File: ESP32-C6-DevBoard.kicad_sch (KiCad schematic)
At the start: 49 parts, among them J1 USB_C_Receptacle_USB2.0_16P, J2 Conn_01x02_Pin, J4 USB_C_Receptacle_USB2.0_16P, J5 Conn_01x16_Pin, J6 Conn_01x16_Pin, Q1 BC847, Q2 BC847, U1 ESP32-C6-MINI-1, U2 CP2104, U3 TLV75801PDRV

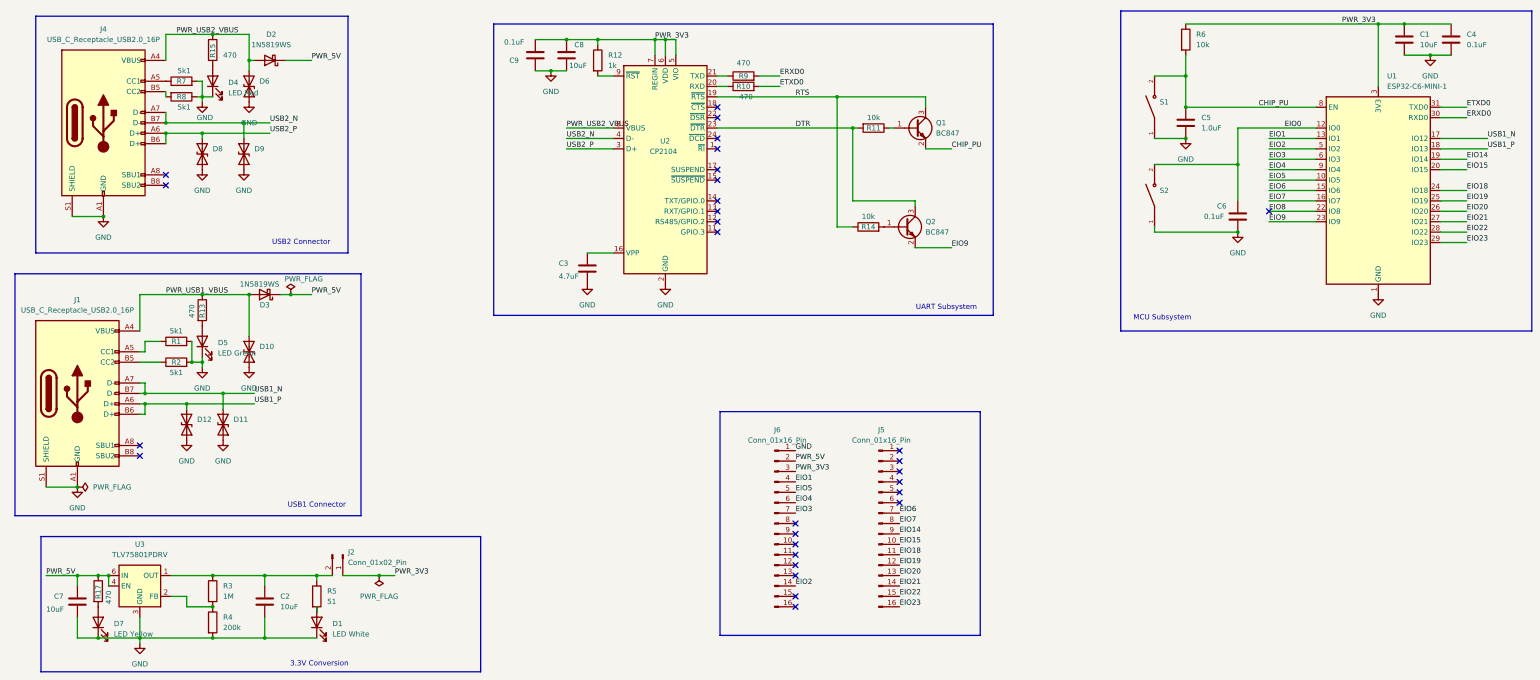
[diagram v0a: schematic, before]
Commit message: Changed to better USB-C connector footprint. Reduced size Changed to 1A 3.3V converter
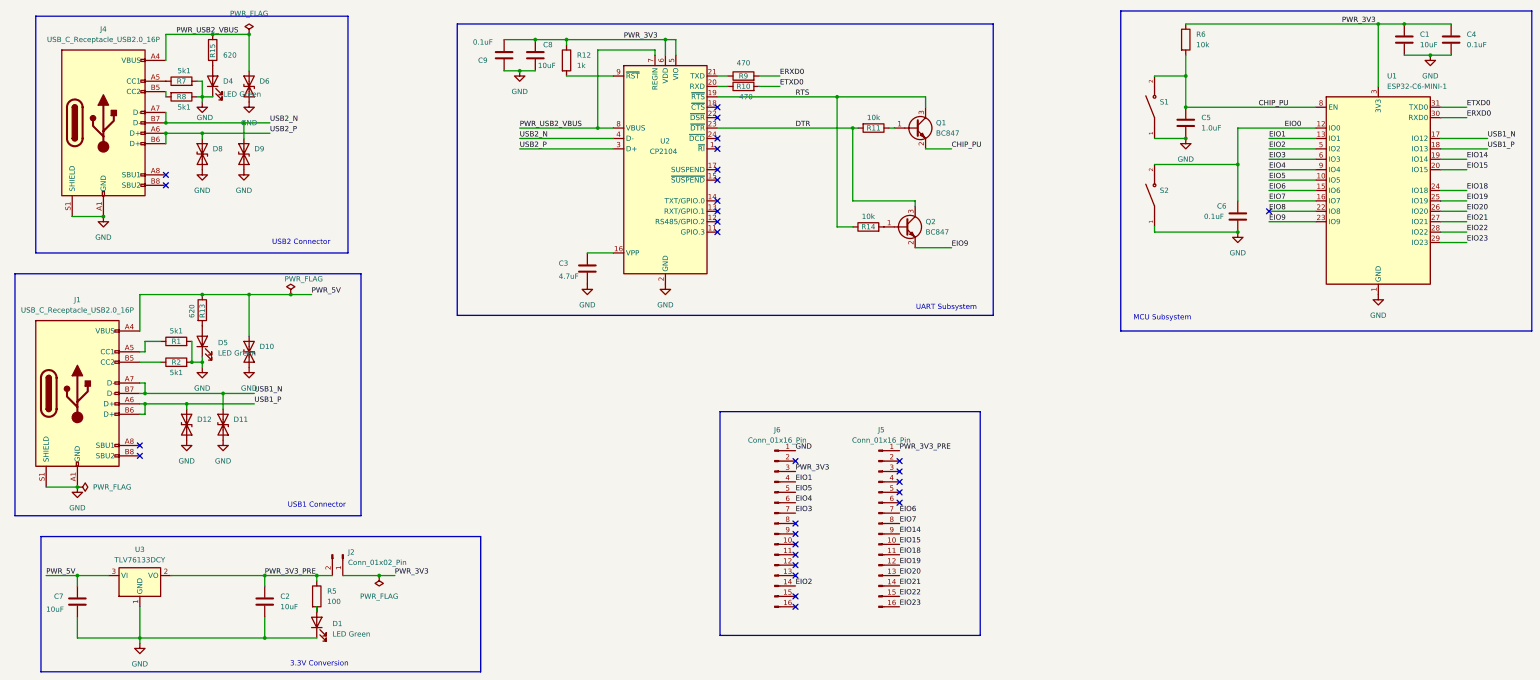
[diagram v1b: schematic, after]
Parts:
- removed D2, D3: 1N5819WS, Diode_SMD:D_SOD-323, symbol Diode:1N5819WS
- removed D7: LED Yellow, LED_SMD:LED_0603_1608Metric, symbol Device:LED
- removed R17: 470, Resistor_SMD:R_0603_1608Metric, symbol Device:R
- removed R3: 1M, Resistor_SMD:R_0603_1608Metric, symbol Device:R
- removed R4: 200k, Resistor_SMD:R_0603_1608Metric, symbol Device:R
- removed U3: TLV75801PDRV, Package_SON:WSON-6-1EP_2x2mm_P0.65mm_EP1x1.6mm, symbol Regulator_Linear:TLV75801PDRV
- added U3: TLV76133DCY, Package_TO_SOT_SMD:SOT-223-3_TabPin2, symbol Regulator_Linear:TLV76133DCY
- D1: value LED White -> LED Green; LCSC C2290 -> C12065; LCSC Part Name C125123 -> C12065
- D4: value LED Red -> LED Green; LCSC C2286 -> C12065; LCSC Part Name C125103 -> C12065
- D5: LCSC C916074 -> C12065
- J1, J4: footprint Connector_USB:USB_C_Receptacle_JAE_DX07S016JA1R1500 -> Connector_USB:USB_C_Receptacle_HRO_TYPE-C-31-M-12
- R13, R15: value 470 -> 620; LCSC C23179 -> C23220; LCSC Part Name C23197 -> C23220
- R5: value 51 -> 100; LCSC C23197 -> C22775; LCSC Part Name C23197 -> C22775
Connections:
- net PWR_USB1_VBUS is gone; now on net PWR_5V: D10.2 (A2), J1.A4 (VBUS), J1.A9 (VBUS), J1.B4 (VBUS), J1.B9 (VBUS), R13.1
- net GND: now also U3.1 (GND)
- net PWR_3V3: no longer U2.7 (REGIN)
- net PWR_5V: now also U3.3 (VI); no longer J6.2 (Pin_2)
- net PWR_USB2_VBUS: now also U2.7 (REGIN)
- net PWR_3V3_PRE: now reaches C2.1, J2.2 (Pin_2), R5.1
- net PWR_3V3_PRE: now also J5.1 (Pin_1), U3.2 (VO)
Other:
- moved on the sheet: C8, C9, R12

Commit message: Further improvements
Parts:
- C1, C2, C7, C8: LCSC Part Name C96446 -> (none)
- C3: LCSC Part Name C19666 -> (none)
- C4, C6, C9: LCSC Part Name C30926 -> (none)
- C5: LCSC Part Name C15849 -> (none)
- D1, D4, D5: LCSC Part Name C12065 -> (none)
- D10, D11, D12, D6, D8, D9: LCSC Part Name C502527 -> (none)
- J1, J4: LCSC Part Name C2765186 -> (none)
- J2: LCSC Part Name C124375 -> (none)
- J5, J6: LCSC Part Name C25503134 -> (none)
- Q1, Q2: LCSC Part Name C57668 -> (none)
- R1, R2, R7, R8: LCSC Part Name C23186 -> (none)
- R10, R9: LCSC Part Name C23197 -> (none)
- R11, R14, R6: LCSC Part Name C25804 -> (none)
- R12: LCSC Part Name C23179 -> (none)
- R13, R15: LCSC Part Name C23220 -> (none)
- R5: LCSC Part Name C22775 -> (none)
- S1, S2: LCSC Part Name C720477 -> (none)
- U1: LCSC Part Name C5736265 -> (none)
- U2: LCSC Part Name C47742 -> (none)

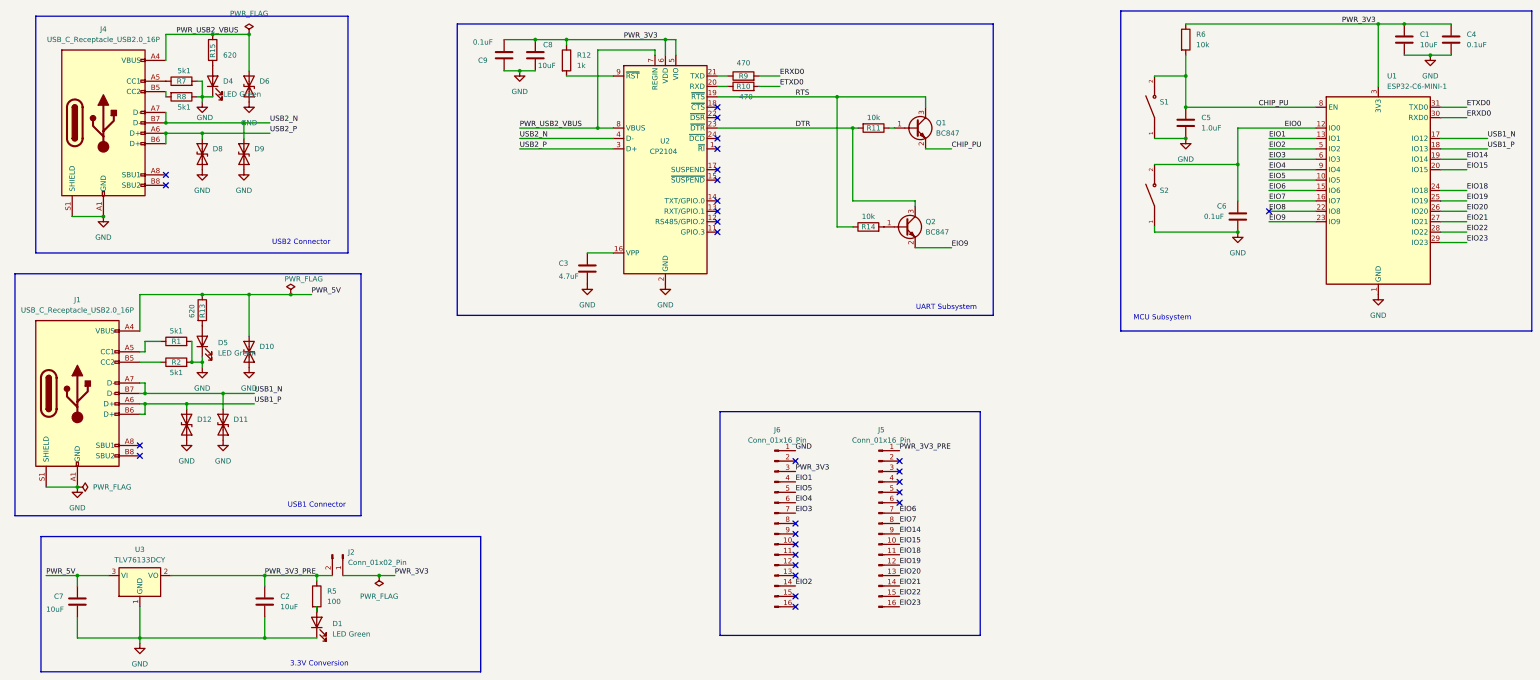
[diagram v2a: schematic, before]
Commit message: Change to unidirectional diodes (as that is what I actuallt ordered)
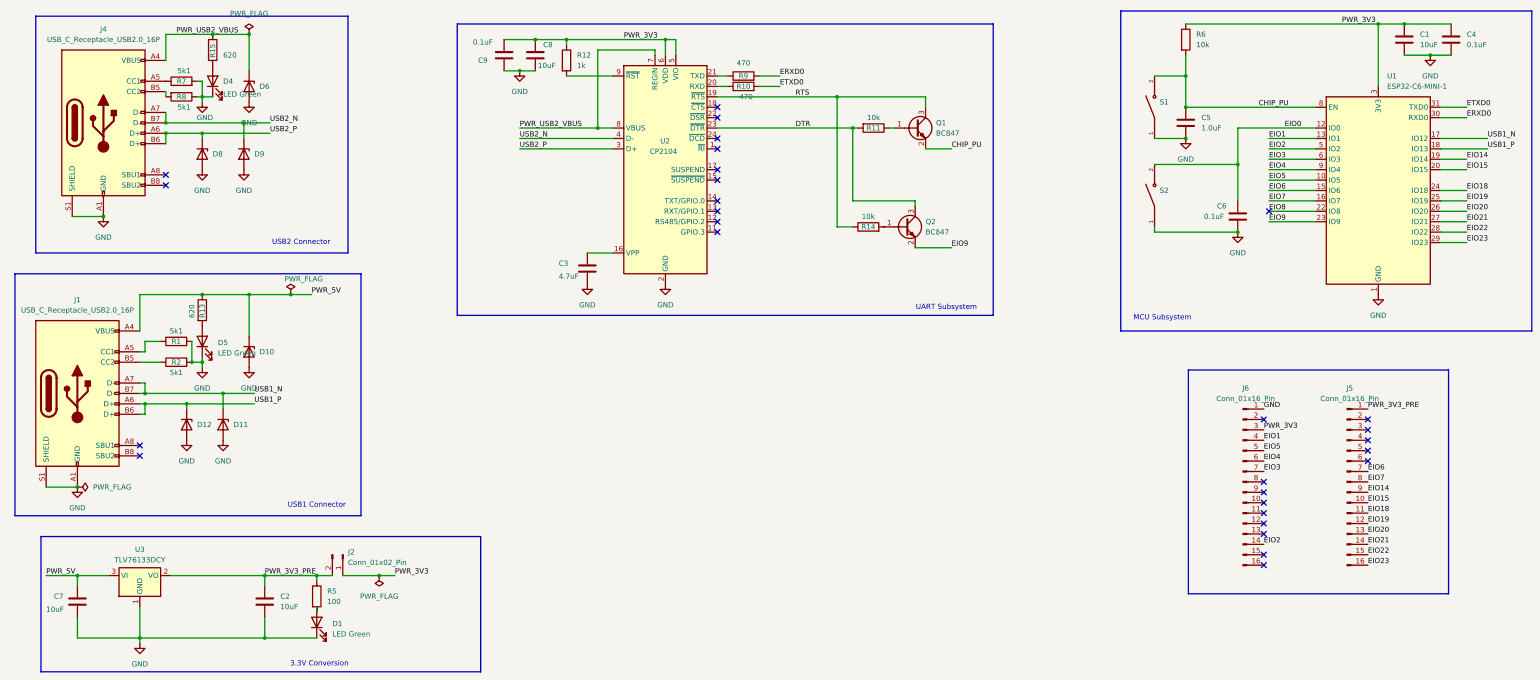
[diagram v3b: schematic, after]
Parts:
- D10, D11, D12, D6, D8, D9: footprint Diode_SMD:D_SOD-323 -> Diode_SMD:D_SOD-882; symbol Diode:SD05_SOD323 -> Diode:PESD5V0S1UL
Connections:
- net GND: now also D10.2 (A), D11.2 (A), D12.2 (A), D6.2 (A), D8.2 (A), D9.2 (A); no longer D10.1 (A1), D11.1 (A1), D12.1 (A1), D6.1 (A1), D8.1 (A1), D9.1 (A1)
- net PWR_5V: now also D10.1 (K); no longer D10.2 (A2)
- net PWR_USB2_VBUS: now also D6.1 (K); no longer D6.2 (A2)
- net USB1_N: now also D11.1 (K); no longer D11.2 (A2)
- net USB1_P: now also D12.1 (K); no longer D12.2 (A2)
- net USB2_N: now also D9.1 (K); no longer D9.2 (A2)
- net USB2_P: now also D8.1 (K); no longer D8.2 (A2)
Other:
- moved on the sheet: J5, J6
